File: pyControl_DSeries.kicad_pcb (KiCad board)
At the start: 2 copper layers, 90.2 x 66.5 mm, 14 parts, among them J1 Barrel_Jack, J2 RJ45-12PORT, U1 PyBoard-D-Series, U2 MC7805_DPAK, U3 TBD62083APG, U4 TBD62083APG, U5 TBD62083APG

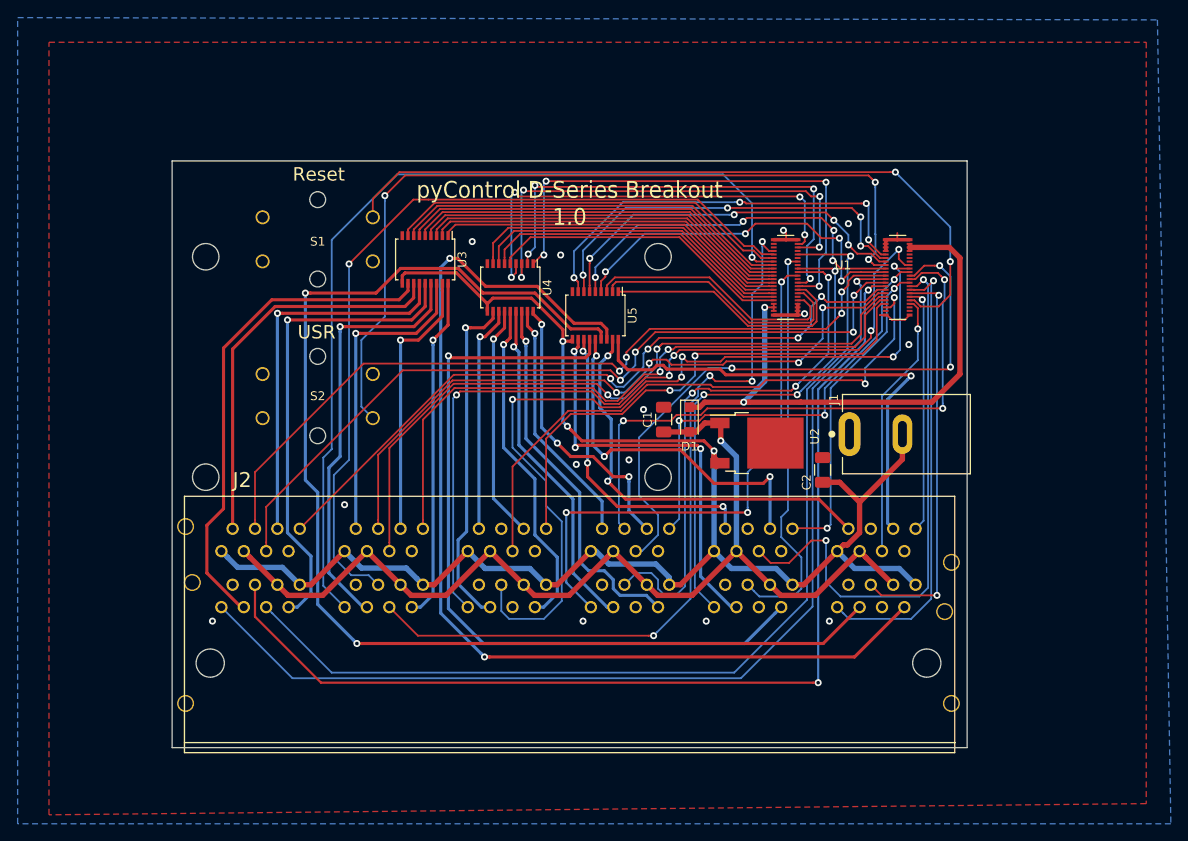
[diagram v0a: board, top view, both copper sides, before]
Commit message: rev 1.1 fixed pins on dc jack and linear regulator. connected T3_DC repositioned DIN adapters added BOM and datasheets
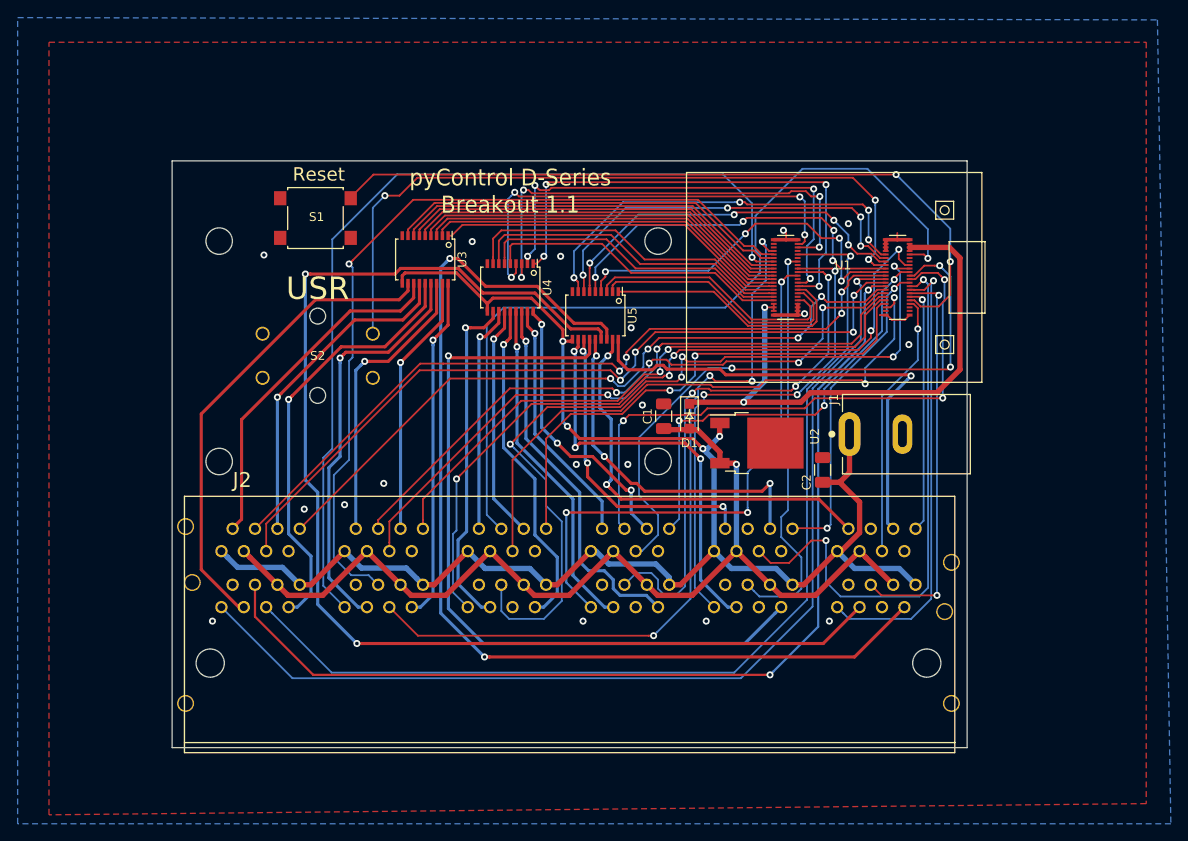
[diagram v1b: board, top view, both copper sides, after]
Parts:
- S1: footprint Andy_footprints:12mm_tactile_SPST -> Andy_footprints:6mm_tactile_smd
- moved S2 4.57 mm to (68.6, 108.0)
- moved S1 2.43 mm to (68.3, 92.3)
- moved DRA1 2.34 mm to (57.4, 107.4)
- moved DRA2 1.78 mm to (107.2, 107.4)
- moved C1 0.38 mm to (107.8, 114.8)
- moved D1 0.38 mm to (110.7, 114.8)
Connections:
- J1 pad 1: /GND -> /12VDC
- J1 pad 2: /12VDC -> /GND
- J2 pad T3-5: (no net) -> /T3_DC
- S1 pad 2: (no net) -> /GND
- S2 pad 1: /USR -> /GND
- S2 pad 2: (no net) -> /GND
- S2 pad 3: /GND -> /USR
- U1 pad 74: (no net) -> /T3_DC
- U2 pad 1: /5VDC -> /12VDC
- U2 pad 3: /12VDC -> /5VDC
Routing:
- net /T3_DC: track 0.00 -> 94.2 mm, vias 0 -> 1
- net /USR: track 95.1 -> 83.0 mm
- net /B3_DA: track 90.7 -> 84.0 mm
- net /T2_DA: track 74.1 -> 67.6 mm
- net /T2_DB: track 78.9 -> 73.0 mm
- net /T1_PA: track 43.3 -> 37.7 mm
- net /B1_PB: track 54.2 -> 48.7 mm
- net /T1_PB: track 45.0 -> 39.7 mm
- net /T2_DC: track 77.7 -> 72.6 mm
- net /B1_DB: track 119.7 -> 115.2 mm
- net /12VDC: track 187.4 -> 183.6 mm, vias 3 -> 4
- net /T1_DC: track 90.4 -> 86.7 mm
- net /B3_DB: track 96.6 -> 93.3 mm
- net /T2_PB: track 35.7 -> 33.2 mm
- net /B1_PA: track 56.6 -> 54.3 mm
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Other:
- rule pad_to_mask_clearance: 0.0508 -> 0.2032
- rule via_min_drill: 0.3 -> 0.2032
- rule via_min_size: 0.4 -> 0.4572
- board text added: "pyControl D-Series Breakout 1.1"
- board text removed: "pyControl D-Series Breakout 1.0"
